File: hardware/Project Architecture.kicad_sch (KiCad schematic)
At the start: 0 parts

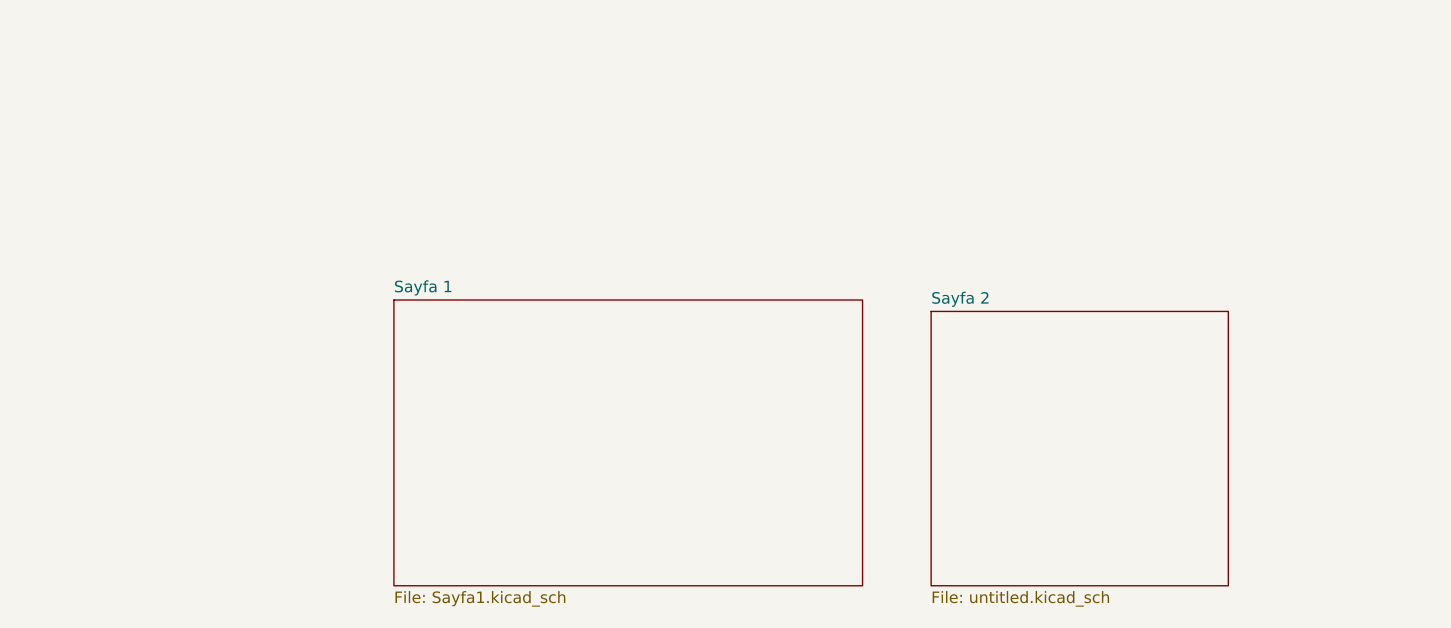
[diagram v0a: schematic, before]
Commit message: docs(readme): güncel proje yapısını ve kullanımını belgele
README'yi hiyerarşik şematikler, proje değişkenleri, BOM ve net ayarlarıyla güncelle. Üretim ve CI davranışını açıklığa kavuştur.
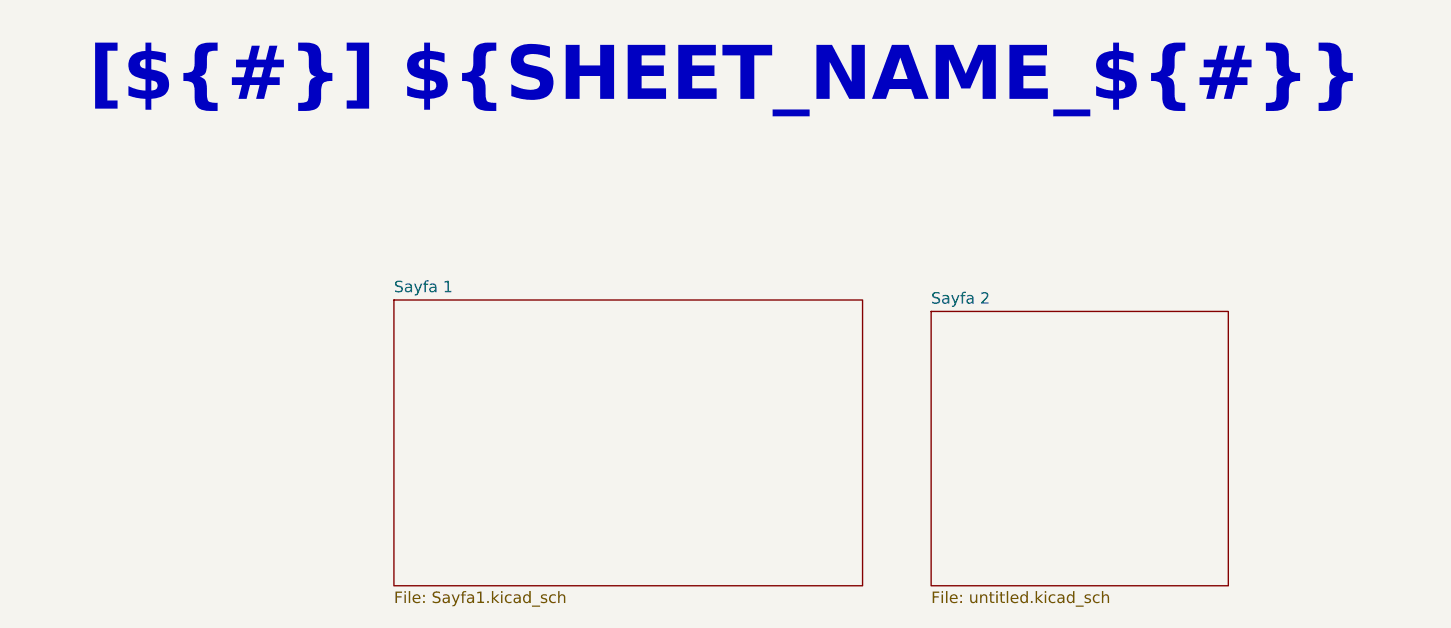
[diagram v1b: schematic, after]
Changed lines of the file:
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@@
 	(generator_version "10.0")
 	(paper "A3")
+	(text_box "[${#}] ${SHEET_NAME_${#}}"
+		(exclude_from_sim no)
+		(at 140.97 24.13 0)
+		(size 137.16 18.3317)
+		(margins 4.4999 4.4999 4.4999 4.4999)
+		(stroke
+			(width -0.0001)
+			(type solid)
+		)
+		(fill
+			(type none)
+		)
+		(effects
+			(font
+				(face "Times New Roman")
+				(size 6 6)
+				(thickness 1.2)
+				(bold yes)
+				(color 162 22 34 1)
+			)
+		)
+	)
 	(sheet
 		(at 172.72 58.42)
